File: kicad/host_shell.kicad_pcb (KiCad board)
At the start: 2 copper layers, 90 x 100 mm, 241 parts, among them J1 FG PH-2AWT, J10 Memory Card Slot, J11 Conn_02x12_Odd_Even, J2 Conn_01x02, J3 Conn_01x02, J4 Conn_01x40, J5 Conn_02x10_Odd_Even, J6 Conn_01x03, J7 Conn_01x02, J8 PJ-316A-6A, J9 Conn_01x02, P1 TYPE-C16PIN, Q1 IRLML2246TRPBF, Q4 BSS138W, Q5 BSS84W, Q6 BSS138W, Q7 BSS138W, SW1 GT-TC018A-H0375-L1, SW10 PTS645SL50SMTR92, SW11 SKRPACE010_6, SW12 PTS645SL50SMTR92, SW13 PTS645SL50SMTR92, SW2 PTS645SL50SMTR92, SW3 PTS645SL50SMTR92, SW4 PTS645SL50SMTR92, SW5 PTS645SL50SMTR92, SW6 PTS645SL50SMTR92, SW7 PTS645SL50SMTR92, SW8 PTS645SL50SMTR92, SW9 PTS645SL50SMTR92, U1 MCP73831-2-OT, U10 LM4880MX/NOPB, U11 LM4890S, U12 SN74LVC1G3157DBVR, U13 SN74AHC541PWR, U14 TPS22919DCKR, U15 RV-3028-C7, U2 XC6194AA03ER-G, U3 TPS63802, U4 PCA9555PW, U5 W25Q32JVSSIQ, U6 APS6404L-3SQRx-SN, U7 RP2350B, U8 74LVC2G17GW, U9 LM4890S, Y1 ABM8-272-T3

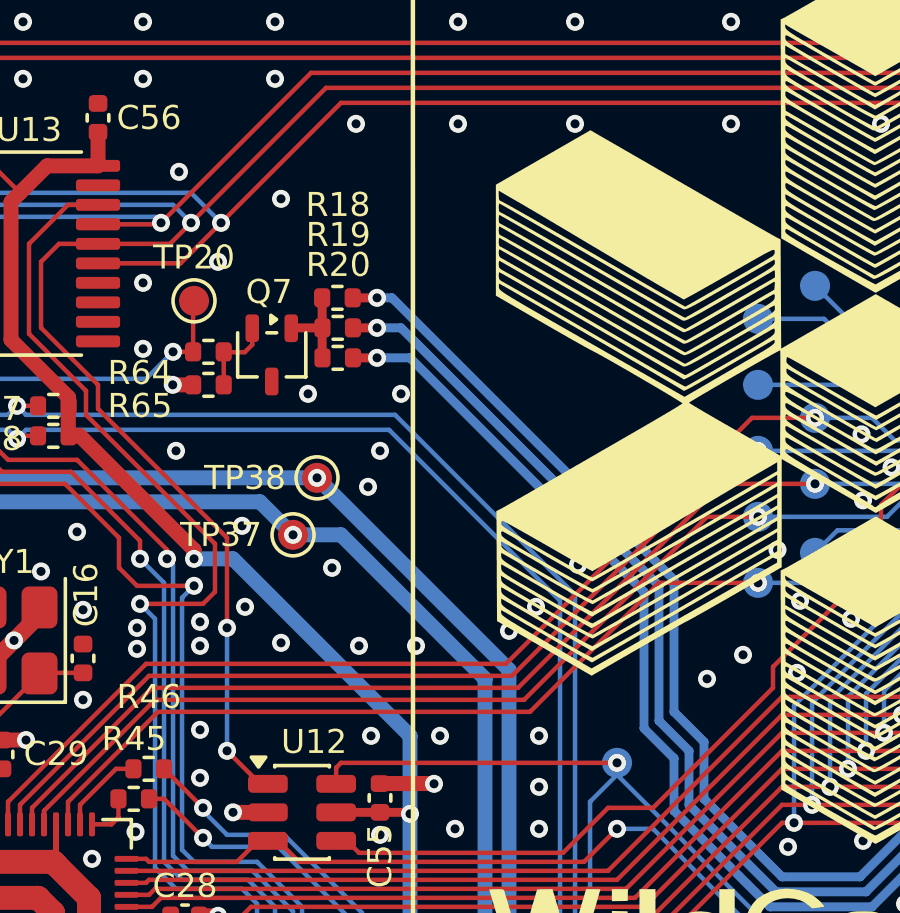
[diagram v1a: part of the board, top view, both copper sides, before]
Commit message: fix footprint
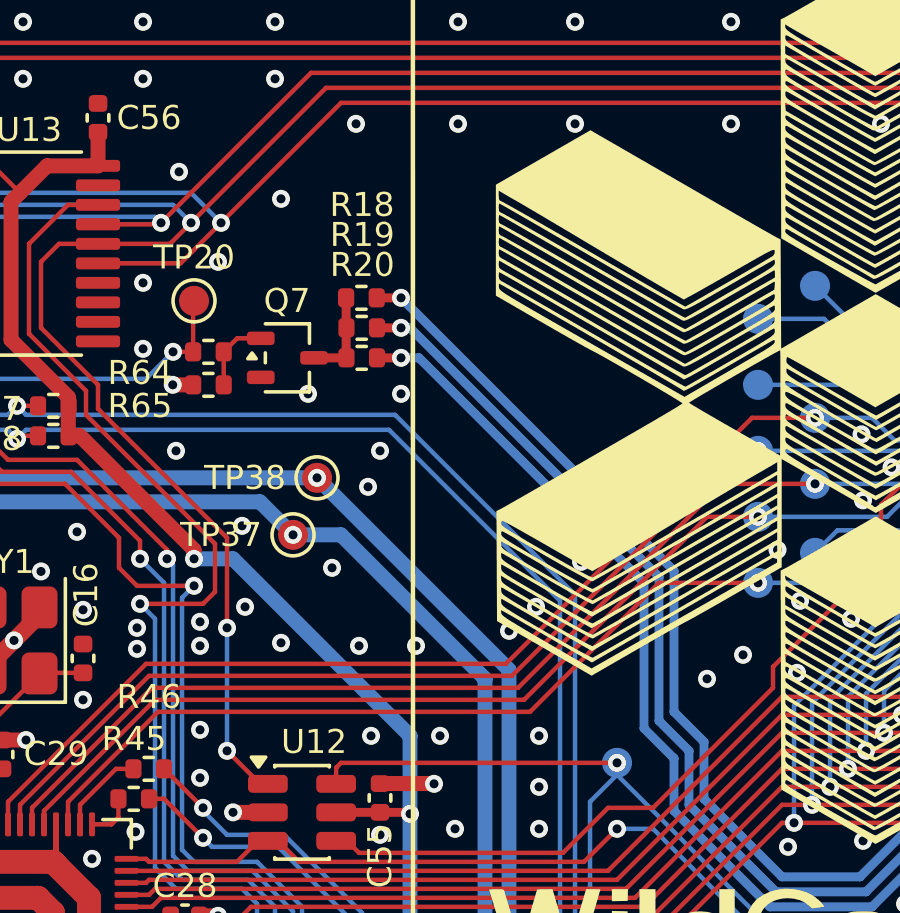
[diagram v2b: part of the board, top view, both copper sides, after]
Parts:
- moved R19 0.80 mm to (82.8, 69.5)
- moved R20 0.80 mm to (82.8, 70.5)
- moved R18 0.80 mm to (82.8, 68.5)
- moved Q7 0.53 mm to (80.3, 70.5), turned to 0 degrees
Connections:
- Q7 pad 1: /HSLCD_BL_K -> Net-(Q7-G)
- Q7 pad 2: Net-(Q7-G) -> GND
- Q7 pad 3: GND -> /HSLCD_BL_K
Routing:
- net Net-(J4-Pin_34): track 33.0 -> 32.4 mm
- net Net-(J4-Pin_36): track 32.6 -> 31.9 mm
- net Net-(J4-Pin_35): track 32.8 -> 32.1 mm

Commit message: rev.1 PCBA ordered
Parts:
- TP37, TP38: moved to B.Cu
- moved TP10 5.37 mm to (93.0, 70.3)
- moved TP30 5.37 mm to (93.0, 76.9)
- moved TP32 5.37 mm to (93.0, 74.7)
- moved TP12 5.36 mm to (93.0, 72.5)
- moved TP14 5.34 mm to (93.0, 79.1)
- moved J4 5.00 mm to (100.0, 79.5)
- moved TP11 2.46 mm to (94.9, 71.4)
- moved TP28 2.46 mm to (94.9, 80.2)
- moved TP29 2.46 mm to (94.9, 78.0)
- moved TP31 2.46 mm to (94.9, 75.8)
- moved TP13 2.46 mm to (94.9, 73.6)
- moved R10 1.93 mm to (113.0, 126.1), turned to -90 degrees
- moved TP9 1.40 mm to (89.9, 84.0)
- moved TP5 1.39 mm to (95.5, 132.6)
- moved TP22 1.30 mm to (58.3, 61.8)
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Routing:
- net 3V3: track 531.7 -> 541.1 mm, vias 24 -> 23
- net Net-(J4-Pin_35): track 32.1 -> 24.9 mm
- net Net-(J4-Pin_34): track 32.4 -> 25.1 mm
- net Net-(J4-Pin_36): track 31.9 -> 24.7 mm
- net /HSLCD_VSYNC: track 38.5 -> 33.2 mm
- net Net-(J4-Pin_2): track 7.58 -> 3.73 mm
- net /HSLCD_SPIEN: track 79.4 -> 76.2 mm
- net /HSLCD_DCCK: track 28.1 -> 25.6 mm
- net Net-(J4-Pin_4): track 7.21 -> 4.75 mm
- net GND: track 40.5 -> 38.1 mm, vias 609 -> 646
- net Net-(U7-RUN): track 28.8 -> 30.7 mm
- net VBAT: track 107.3 -> 109.1 mm
- net /HSLCD_MISO: track 5.56 -> 7.16 mm
- net /3V3PG: track 20.8 -> 19.6 mm
- net /SPKEN: track 123.5 -> 122.5 mm
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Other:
- board text added: "Host Shell Rev.1"
- board text added: "POWER"
- board text added: "RESET"
